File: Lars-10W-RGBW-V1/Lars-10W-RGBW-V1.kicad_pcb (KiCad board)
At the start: 4 copper layers, 47.1 x 43.3 mm, 133 parts, among them J1 USB_C_Receptacle_USB2.0_16P, J101 Conn_Coaxial, J601 Screw_Terminal_01x02, SW1 SW_SPST, SW2 SW_SPST, U1 CH224D, U101 ESP32-C6FHx, U202 TPS92201, U302 TPS92201, U402 TPS92201, U502 TPS92201, U601 MB34F, U602 SY8366H, U603 XBL1117, Y1 40MHz

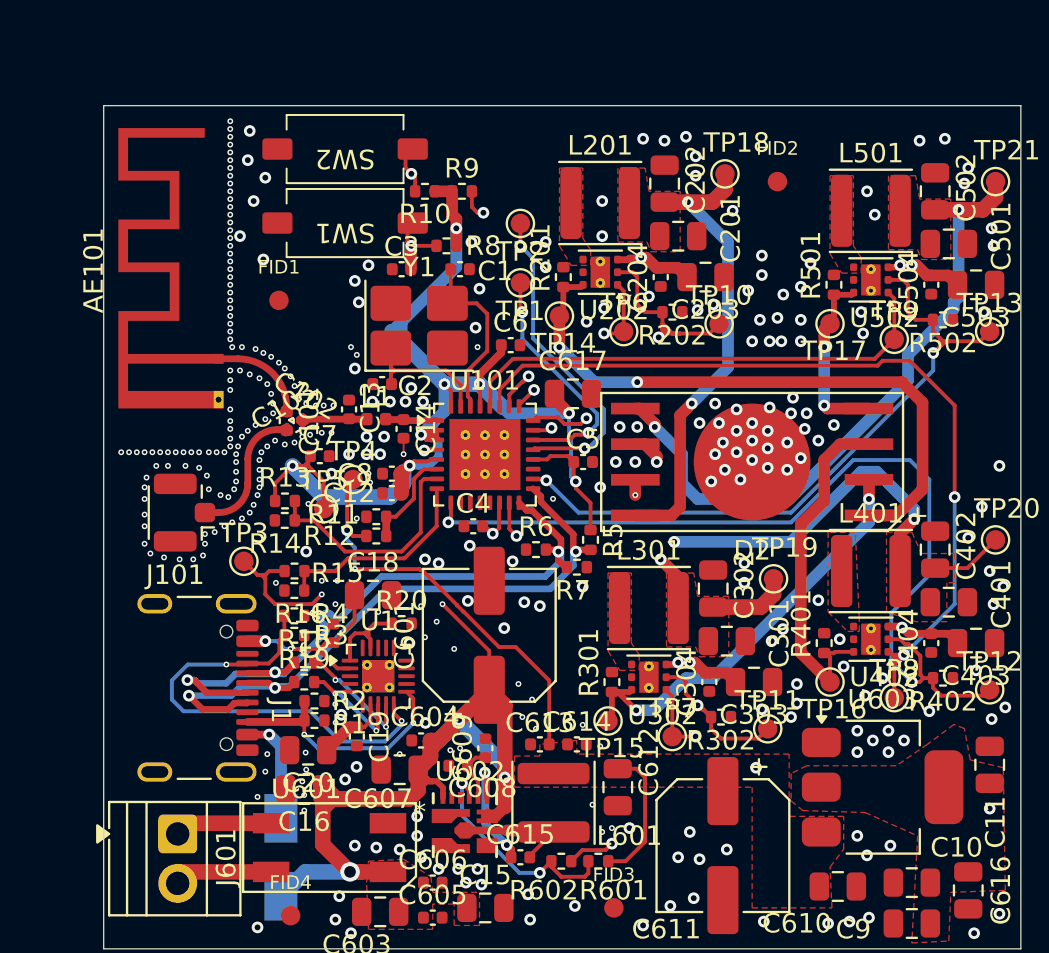
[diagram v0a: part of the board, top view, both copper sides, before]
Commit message: Fixed via sizes
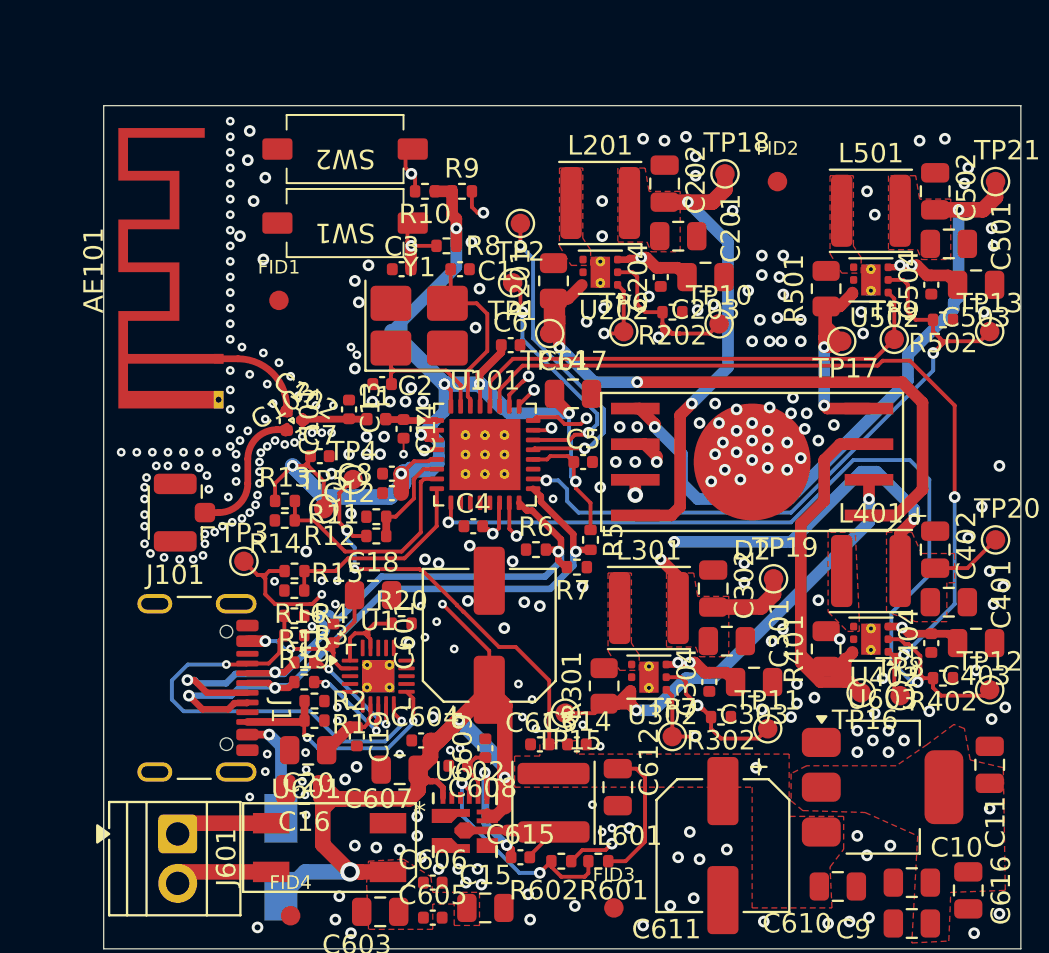
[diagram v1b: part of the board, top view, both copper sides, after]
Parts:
- R201, R301, R401, R501: footprint Resistor_SMD:R_0402_1005Metric -> Resistor_SMD:R_0805_2012Metric
- moved TP15 2.24 mm to (128.8, 69.7)
- moved TP16 1.69 mm to (144.0, 68.7)
- moved TP17 1.08 mm to (143.0, 50.6)
- moved TP14 1.03 mm to (128.0, 50.2)
- moved R201 0.54 mm to (128.2, 47.5)
- moved R501 0.45 mm to (142.2, 47.9)
- moved R301 0.45 mm to (130.8, 68.3)
- moved TP1 0.40 mm to (126.1, 47.6)
- moved TP8 0.32 mm to (146.0, 68.8)
- moved R401 0.32 mm to (142.2, 66.4)
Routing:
- net /LedDriverRed/LED-: track 31.5 -> 37.5 mm
- net /LedDriverBlue/LED-: track 18.3 -> 23.3 mm
- net /LedDriverWhite/LED-: track 9.04 -> 13.3 mm
- net +3V3: track 106.2 -> 109.9 mm
- net /LedDriverGreen/LED-: track 22.1 -> 24.9 mm
- net GND: vias 339 -> 290
